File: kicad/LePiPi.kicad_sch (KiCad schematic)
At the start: 105 parts, among them J1 Conn_01x03_Female, J2 Conn_01x04_Female, SW1 SW_Push, SW10 SW_Push, SW11 SW_Push, SW12 SW_Push, SW13 SW_Push, SW14 SW_Push, SW15 SW_Push, SW16 SW_Push, SW17 SW_Push, SW18 SW_Push, SW19 SW_Push, SW2 SW_Push, SW20 SW_Push, SW21 SW_Push, SW22 SW_Push, SW23 SW_Push, SW24 SW_Push, SW25 SW_Push, SW26 SW_Push, SW27 SW_Push, SW28 SW_Push, SW29 SW_Push, SW3 SW_Push, SW30 SW_Push, SW31 SW_Push, SW32 SW_Push, SW33 SW_Push, SW34 SW_Push, SW35 SW_Push, SW36 Rotary_Encoder_Switch, SW37 SW_Push, SW4 SW_Push, SW5 SW_Push, SW6 SW_Push, SW7 SW_Push, SW8 SW_Push, SW9 SW_Push, U1 ATmega32U4-AU, Y1 Crystal_GND2

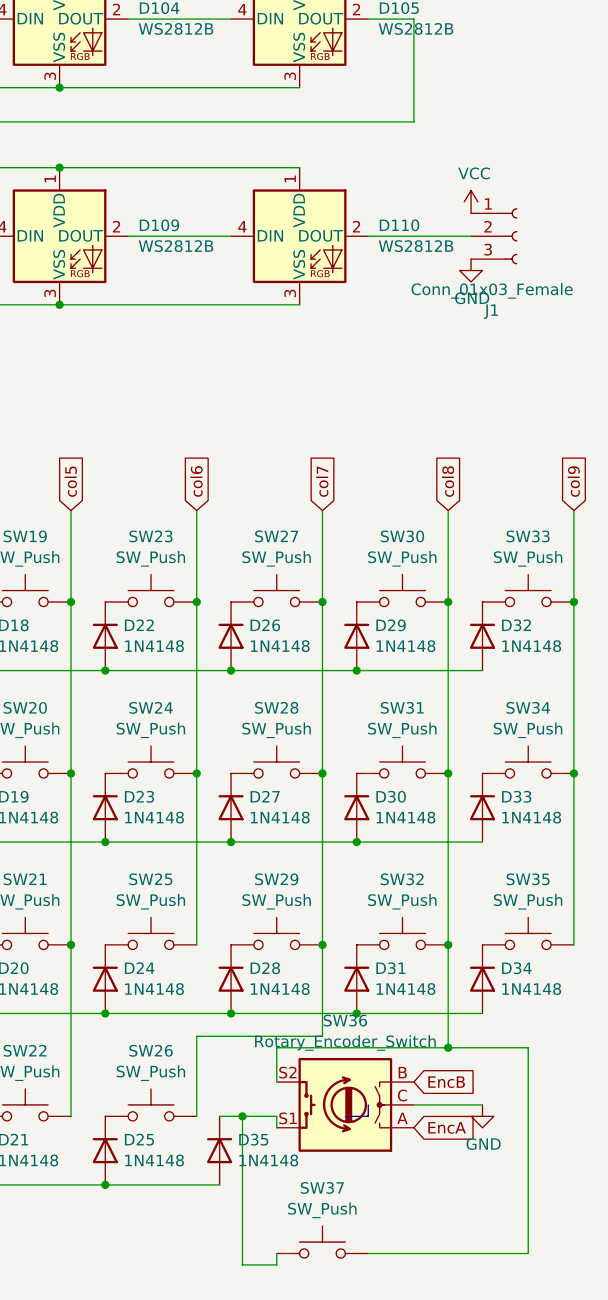
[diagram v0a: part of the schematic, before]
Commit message: replaced switch footprints and removed all routing
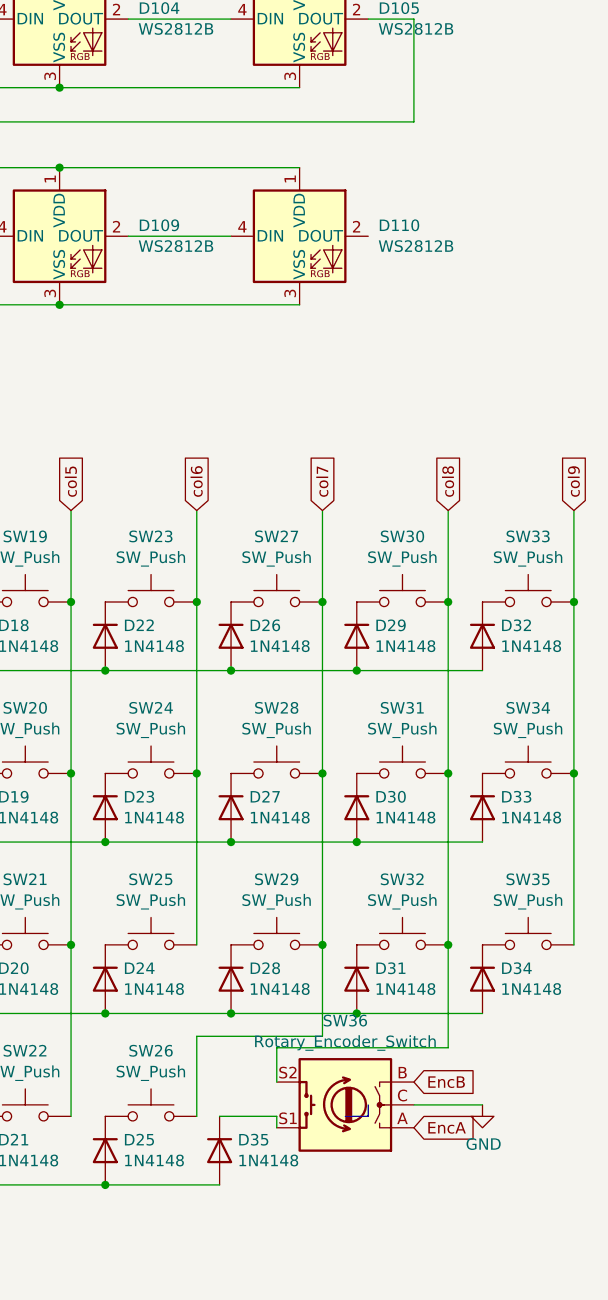
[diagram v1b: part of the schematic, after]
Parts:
- removed J1: Conn_01x03_Female, Connector_PinSocket_2.54mm:PinSocket_1x03_P2.54mm_Vertical, symbol Connector:Conn_01x03_Female
- removed SW37: SW_Push, Keebio-Parts:MX-Alps-Choc-1U-NoLED, symbol Switch:SW_Push
- SW10, SW11, SW12, SW13, SW14, SW15, SW16, SW17, SW19, SW2, SW20, SW21, SW23, SW24, SW25, SW26, SW27, SW28, SW29, SW3, SW30, SW31, SW32, SW33, SW34, SW35, SW4, SW5, SW6, SW7, SW8, SW9: footprint Keebio-Parts:MX-Alps-Choc-1U-NoLED -> 0xcb:SW_Hotswap_Kailh_1.00u
- SW18, SW22: footprint Keebio-Parts:MX-Alps-Choc-2U-StabFlip -> 0xcb:SW_Hotswap_Kailh_2.00u
